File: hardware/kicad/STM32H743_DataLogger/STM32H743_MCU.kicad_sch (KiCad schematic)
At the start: 29 parts, among them J10 SWD Debug, J11 USB-C, U10 STM32H743VIT6, Y1 25MHz, Y2 32.768kHz

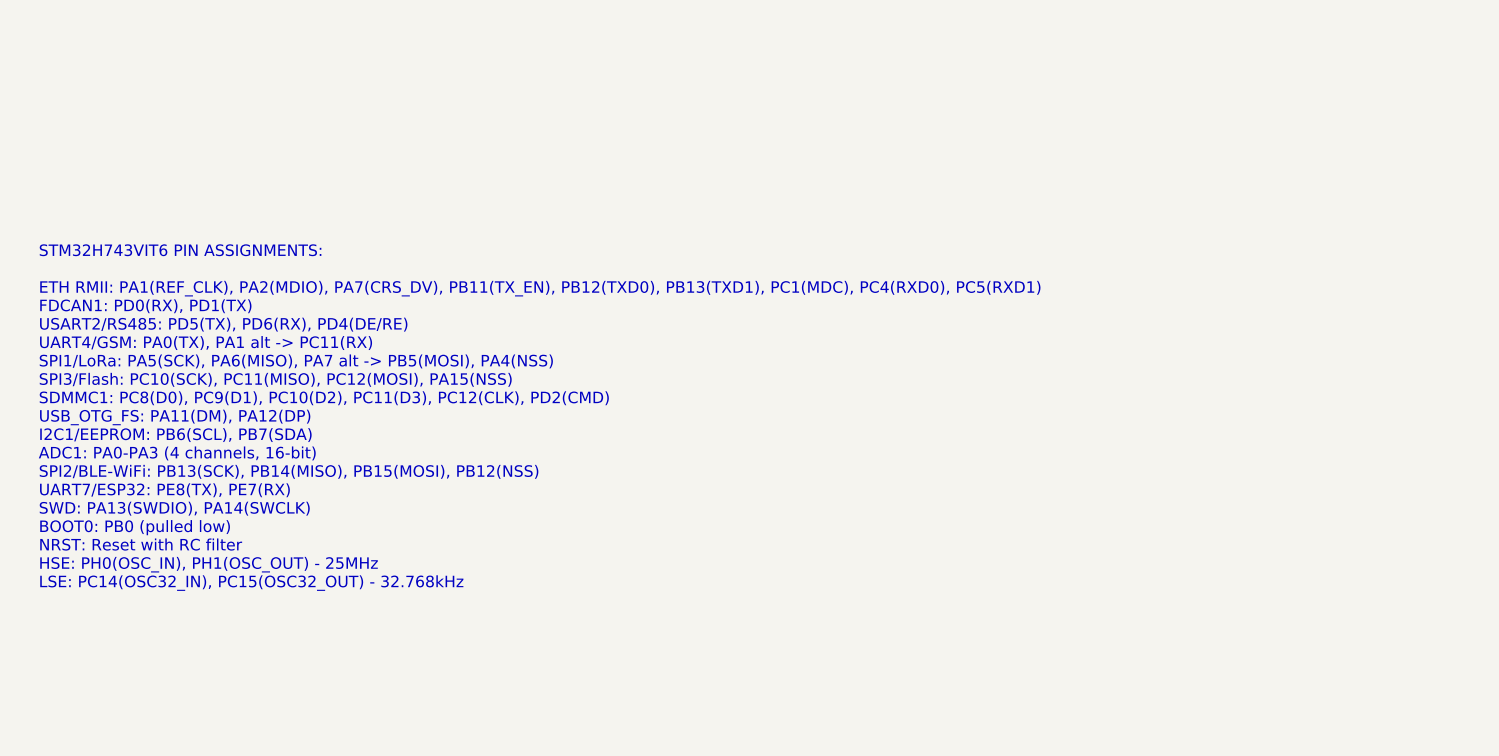
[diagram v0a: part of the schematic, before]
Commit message: feat: Upgrade to full industrial-grade components and SPI architecture
Major design changes for PLC-grade reliability:

Component Upgrades:
- Replace ESP32-C3 dual-MCU with ATWINC1500 WiFi (SPI2) + RN4870 BLE (UART7)
  Eliminates second processor, both rated -40 to +85°C industrial
- Replace LAN8742A RMII PHY with W5500 SPI Ethernet controller
  Hardwired TCP/IP stack, frees 11 RMII pins, simpler firmware
- Replace RFM95W module with SX1276IMLTRT bare IC (-40 to +85°C)
  Full industrial temp range with 32MHz TCXO and custom RF matching
- Add TPS3823-33 external hardware watchdog (1.6s timeout)

Industrial Compliance:
- All key ICs rated -40 to +85°C (industrial grade)
- HumiSeal 1B73 conformal coating spec (MIL-I-46058C)
- EMC compliance targets: IEC 61000-4-2/4/5/6/8
- Ferrite beads on Ethernet pairs for EMI

Architecture: Single MCU (STM32H743) with all peripherals as SPI/UART slaves
- SPI1: SX1276 LoRa
- SPI2: ATWINC1500 WiFi
- SPI3: W25Q64JV Flash
- SPI4: W5500 Ethernet
- UART4: SIM7600G-H GSM/LTE
- UART7: RN4870 BLE

Updated BOM: ~170 components, ~$142/unit (1pc), ~$90/unit (100pc)

https://claude.ai/code/session_01XsiZ6LJT6X46LKY8yEbRbx
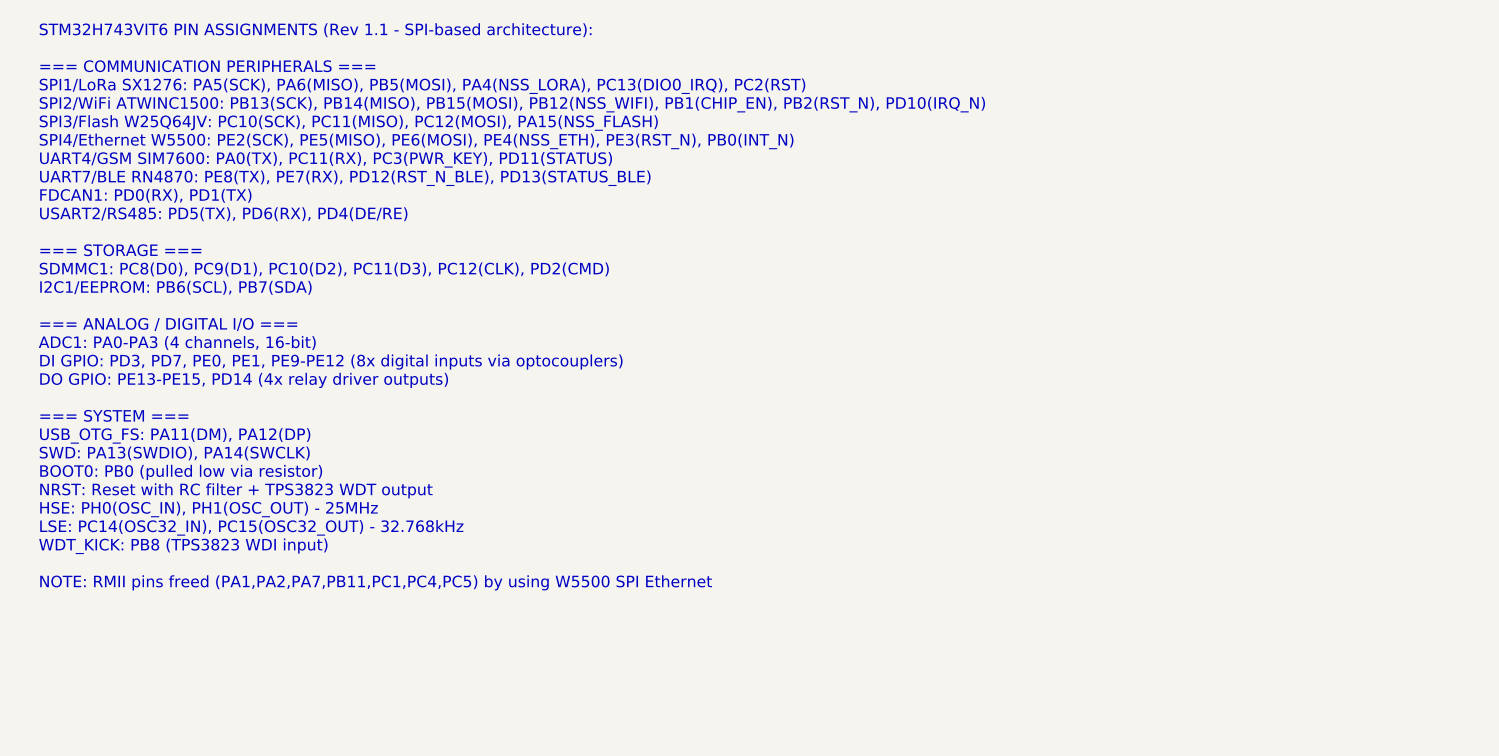
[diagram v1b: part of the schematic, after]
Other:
- note added: "STM32H743VIT6 PIN ASSIGNMENTS (Rev 1.1 - SPI-based architecture): === COMMUNICATION PERIPHERALS === SPI1/LoRa SX1276: PA5(SCK), PA6(MISO), PB5(MOSI), PA4(NSS_LORA), PC13(DIO0_IRQ), PC2(RST) SPI2/WiFi ATWINC1500: PB13(SCK), PB14(MISO), PB15(MOSI), PB12(NSS_WIFI), PB1(CHIP_EN), PB2(RST_N), PD10(IRQ_N) SPI3/Flash W25Q64JV: PC10(SCK), PC11(MISO), PC12(MOSI), PA15(NSS_FLASH) SPI4/Ethernet W5500: PE2(S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"
- note removed: "STM32H743VIT6 PIN ASSIGNMENTS: ETH RMII: PA1(REF_CLK), PA2(MDIO), PA7(CRS_DV), PB11(TX_EN), PB12(TXD0), PB13(TXD1), PC1(MDC), PC4(RXD0), PC5(RXD1) FDCAN1: PD0(RX), PD1(TX) USART2/RS485: PD5(TX), PD6(RX), PD4(DE/RE) UART4/GSM: PA0(TX), PA1 alt -> PC11(RX) SPI1/LoRa: PA5(SCK), PA6(MISO), PA7 alt -> PB5(MOSI), PA4(NSS) SPI3/Flash: PC10(SCK), PC11(MISO), PC12(MOSI), PA15(NSS) SDMMC1: PC8(D0), PC9(D1)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"
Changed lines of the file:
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@@
     (title "STM32H743VIT6 MCU - Core System")
     (date "2026-03-15")
-    (rev "1.0")
+    (rev "1.1")
     (company "SCADA Systems")
     (comment 1 "ARM Cortex-M7 480MHz, 2MB Flash, 1MB RAM")
-    (comment 2 "LQFP-100 package")
+    (comment 2 "LQFP-100 package, SPI-based peripherals (W5500/ATWINC1500/SX1276/RN4870)")
   )
   ;; ============================================================
@@
   ;; PIN ASSIGNMENTS (documented as text annotation)
   ;; ============================================================
-  (text "STM32H743VIT6 PIN ASSIGNMENTS:\n\nETH RMII: PA1(REF_CLK), PA2(MDIO), PA7(CRS_DV), PB11(TX_EN), PB12(TXD0), PB13(TXD1), PC1(MDC), PC4(RXD0), PC5(RXD1)\nFDCAN1: PD0(RX), PD1(TX)\nUSART2/RS485: PD5(TX), PD6(RX), PD4(DE/RE)\nUART4/GSM: PA0(TX), PA1 alt -> PC11(RX)\nSPI1/LoRa: PA5(SCK), PA6(MISO), PA7 alt -> PB5(MOSI), PA4(NSS)\nSPI3/Flash: PC10(SCK), PC11(MISO), PC12(MOSI), PA15(NSS)\nSDMMC1: PC8(D0), PC9(D1), PC10(D2), PC11(D3), PC12(CLK), PD2(CMD)\nUSB_OTG_FS: PA11(DM), PA12(DP)\nI2C1/EEPROM: PB6(SCL), PB7(SDA)\nADC1: PA0-PA3 (4 channels, 16-bit)\nSPI2/BLE-WiFi: PB13(SCK), PB14(MISO), PB15(MOSI), PB12(NSS)\nUART7/ESP32: PE8(TX), PE7(RX)\nSWD: PA13(SWDIO), PA14(SWCLK)\nBOOT0: PB0 (pulled low)\nNRST: Reset with RC filter\nHSE: PH0(OSC_IN), PH1(OSC_OUT) - 25MHz\nLSE: PC14(OSC32_IN), PC15(OSC32_OUT) - 32.768kHz"
+  (text "STM32H743VIT6 PIN ASSIGNMENTS (Rev 1.1 - SPI-based architecture):\n\n=== COMMUNICATION PERIPHERALS ===\nSPI1/LoRa SX1276: PA5(SCK), PA6(MISO), PB5(MOSI), PA4(NSS_LORA), PC13(DIO0_IRQ), PC2(RST)\nSPI2/WiFi ATWINC1500: PB13(SCK), PB14(MISO), PB15(MOSI), PB12(NSS_WIFI), PB1(CHIP_EN), PB2(RST_N), PD10(IRQ_N)\nSPI3/Flash W25Q64JV: PC10(SCK), PC11(MISO), PC12(MOSI), PA15(NSS_FLASH)\nSPI4/Ethernet W5500: PE2(SCK), PE5(MISO), PE6(MOSI), PE4(NSS_ETH), PE3(RST_N), PB0(INT_N)\nUART4/GSM SIM7600: PA0(TX), PC11(RX), PC3(PWR_KEY), PD11(STATUS)\nUART7/BLE RN4870: PE8(TX), PE7(RX), PD12(RST_N_BLE), PD13(STATUS_BLE)\nFDCAN1: PD0(RX), PD1(TX)\nUSART2/RS485: PD5(TX), PD6(RX), PD4(DE/RE)\n\n=== STORAGE ===\nSDMMC1: PC8(D0), PC9(D1), PC10(D2), PC11(D3), PC12(CLK), PD2(CMD)\nI2C1/EEPROM: PB6(SCL), PB7(SDA)\n\n=== ANALOG / DIGITAL I/O ===\nADC1: PA0-PA3 (4 channels, 16-bit)\nDI GPIO: PD3, PD7, PE0, PE1, PE9-PE12 (8x digital inputs via optocouplers)\nDO GPIO: PE13-PE15, PD14 (4x relay driver outputs)\n\n=== SYSTEM ===\nUSB_OTG_FS: PA11(DM), PA12(DP)\nSWD: PA13(SWDIO), PA14(SWCLK)\nBOOT0: PB0 (pulled low via resistor)\nNRST: Reset with RC filter + TPS3823 WDT output\nHSE: PH0(OSC_IN), PH1(OSC_OUT) - 25MHz\nLSE: PC14(OSC32_IN), PC15(OSC32_OUT) - 32.768kHz\nWDT_KICK: PB8 (TPS3823 WDI input)\n\nNOTE: RMII pins freed (PA1,PA2,PA7,PB11,PC1,PC4,PC5) by using W5500 SPI Ethernet"
     (exclude_from_sim no)
     (at 25.4 25.4 0)

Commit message: feat: Add programming interface headers (J12-J14) to PCB
Schematic additions (STM32H743_MCU.kicad_sch):
- J12: UART debug console header (4-pin 2.54mm: VCC/TX/RX/GND)
  USART1 on PA9(TX)/PA10(RX) at 115200 baud, FTDI cable compatible
  33R series resistors (R14/R15) for ESD protection
- J13: BOOT0 select jumper (3-pin: GND-BOOT0-3V3)
  GND position = normal flash boot (default via R16 10k pull-down)
  3V3 position = DFU bootloader mode for USB/UART programming
- J14: Tag-Connect TC2050-IDC pads (10-pin pogo-pin footprint)
  Same SWD signals as J10, zero per-board connector cost
  For production/factory programming

Firmware additions:
- debug_console.rs: UART console driver with boot banner, periodic
  status reports, log levels, and simple command parser for field
  diagnostics (status/sdinfo/alarms/links/version/reset/help)
- debug_console_task: Embassy async task outputting diagnostics on J12
- uart_ports.rs: Added USART1 debug console config (115200 baud)
- Updated pin assignment docs to Rev 1.2

https://claude.ai/code/session_01XsiZ6LJT6X46LKY8yEbRbx
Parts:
- added J12: UART Debug Console, Connector_PinHeader_2.54mm:PinHeader_1x04_P2.54mm_Vertical, symbol Connector_Generic:Conn_01x04
- added J13: BOOT0 Select, Connector_PinHeader_2.54mm:PinHeader_1x03_P2.54mm_Vertical, symbol Connector_Generic:Conn_01x03
- added J14: TC2050-IDC SWD, Connector:Tag-Connect_TC2050-IDC-FP_2x05_P1.27mm_Vertical, symbol Connector:Tag-Connect_TC2050-IDC
- added R14, R15: 33R, Resistor_SMD:R_0402_1005Metric, symbol Device:R
- added R16: 10k, Resistor_SMD:R_0402_1005Metric, symbol Device:R
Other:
- note added: "STM32H743VIT6 PIN ASSIGNMENTS (Rev 1.2 - SPI-based architecture): === COMMUNICATION PERIPHERALS === SPI1/LoRa SX1276: PA5(SCK), PA6(MISO), PB5(MOSI), PA4(NSS_LORA), PC13(DIO0_IRQ), PC2(RST) SPI2/WiFi ATWINC1500: PB13(SCK), PB14(MISO), PB15(MOSI), PB12(NSS_WIFI), PB1(CHIP_EN), PC0(RST_N), PD10(IRQ_N) SPI3/Flash W25Q64JV: PB3(SCK), PB4(MISO), PB2(MOSI), PA15(NSS_FLASH) [REMAPPED from PC10-12 for SD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"
- note removed: "STM32H743VIT6 PIN ASSIGNMENTS (Rev 1.1 - SPI-based architecture): === COMMUNICATION PERIPHERALS === SPI1/LoRa SX1276: PA5(SCK), PA6(MISO), PB5(MOSI), PA4(NSS_LORA), PC13(DIO0_IRQ), PC2(RST) SPI2/WiFi ATWINC1500: PB13(SCK), PB14(MISO), PB15(MOSI), PB12(NSS_WIFI), PB1(CHIP_EN), PB2(RST_N), PD10(IRQ_N) SPI3/Flash W25Q64JV: PC10(SCK), PC11(MISO), PC12(MOSI), PA15(NSS_FLASH) SPI4/Ethernet W5500: PE2(S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"
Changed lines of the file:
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@@
+  )
+  ;; ============================================================
+  ;; UART DEBUG CONSOLE HEADER (J12)
+  ;; 4-pin 2.54mm header: VCC(3.3V), TX(PA9), RX(PA10), GND
+  ;; USART1 at 115200 baud for debug/diagnostic output
+  ;; Compatible with standard FTDI USB-UART cables
+  ;; ============================================================
+  (symbol
+    (lib_id "Connector_Generic:Conn_01x04")
+    (at 254.0 101.6)
+    (unit 1)
+    (exclude_from_sim no)
+    (in_bom yes)
+    (on_board yes)
+    (dnp no)
+    (uuid "MCU-0090-J12")
+    (property "Reference" "J12"
+      (at 254.0 92.71 0)
+      (effects (font (size 1.27 1.27)))
+    )
+    (property "Value" "UART Debug Console"
+      (at 254.0 95.25 0)
+      (effects (font (size 1.27 1.27)))
+    )
+    (property "Footprint" "Connector_PinHeader_2.54mm:PinHeader_1x04_P2.54mm_Vertical"
+      (at 254.0 101.6 0)
+      (effects (font (size 1.27 1.27)) hide)
+    )
+    (property "MPN" "PinHeader_1x04_P2.54mm"
+      (at 254.0 101.6 0)
+      (effects (font (size 1.27 1.27)) hide)
+    )
+    (property "Manufacturer" "Generic"
+      (at 254.0 101.6 0)
+      (effects (font (size 1.27 1.27)) hide)
+    )
+    (pin "1" (uuid "J12-pin1-uuid") (name "VCC_3V3"))
+    (pin "2" (uuid "J12-pin2-uuid") (name "USART1_TX (PA9)"))
+    (pin "3" (uuid "J12-pin3-uuid") (name "USART1_RX (PA10)"))
+    (pin "4" (uuid "J12-pin4-uuid") (name "GND"))
+  )
+  ;; ESD protection on UART debug header
+  (symbol (lib_id "Device:R") (at 248.92 101.6) (unit 1)
+    (exclude_from_sim no) (in_bom yes) (on_board yes) (dnp no)
+    (uuid "MCU-0091-R14")
+    (property "Reference" "R14" (at 246.38 100.33 0) (effects (font (size 1.27 1.27))))
+    (property "Value" "33R" (at 248.92 104.14 0) (effects (font (size 1.27 1.27))))
+    (property "Footprint" "Resistor_SMD:R_0402_1005Metric" (at 248.92 101.6 0) (effects (font (size 1.27 1.27)) hide))
+    (property "MPN" "RC0402FR-0733RL" (at 248.92 101.6 0) (effects (font (size 1.27 1.27)) hide))
+    (property "Manufacturer" "Yageo" (at 248.92 101.6 0) (effects (font (size 1.27 1.27)) hide))
+  )
+  (symbol (lib_id "Device:R") (at 248.92 107.95) (unit 1)
+    (exclude_from_sim no) (in_bom yes) (on_board yes) (dnp no)
+    (uuid "MCU-0092-R15")
+    (property "Reference" "R15" (at 246.38 106.68 0) (effects (font (size 1.27 1.27))))
+    (property "Value" "33R" (at 248.92 110.49 0) (effects (font (size 1.27 1.27))))
+    (property "Footprint" "Resistor_SMD:R_0402_1005Metric" (at 248.92 107.95 0) (effects (font (size 1.27 1.27)) hide))
+    (property "MPN" "RC0402FR-0733RL" (at 248.92 107.95 0) (effects (font (size 1.27 1.27)) hide))
+    (property "Manufacturer" "Yageo" (at 248.92 107.95 0) (effects (font (size 1.27 1.27)) hide))
+  )
+  ;; ============================================================
+  ;; BOOT0 SELECT HEADER (J13)
+  ;; 1x3 2.54mm jumper: GND-BOOT0-3V3
+  ;; Center pin to BOOT0, jumper to GND=normal flash boot,
+  ;; jumper to 3V3=DFU bootloader mode (USB/UART programming)
+  ;; ============================================================
+  (symbol
+    (lib_id "Connector_Generic:Conn_01x03")
+    (at 254.0 120.65)
+    (unit 1)
+    (exclude_from_sim no)
+    (in_bom yes)
+    (on_board yes)
+    (dnp no)
+    (uuid "MCU-0095-J13")
+    (property "Reference" "J13"
+      (at 254.0 113.03 0)
+      (effects (font (size 1.27 1.27)))
+    )
+    (property "Value" "BOOT0 Select"
+      (at 254.0 115.57 0)
+      (effects (font (size 1.27 1.27)))
+    )
+    (property "Footprint" "Connector_PinHeader_2.54mm:PinHeader_1x03_P2.54mm_Vertical"
+      (at 254.0 120.65 0)
+      (effects (font (size 1.27 1.27)) hide)
+    )
+    (property "MPN" "PinHeader_1x03_P2.54mm"
+      (at 254.0 120.65 0)
+      (effects (font (size 1.27 1.27)) hide)
+    )
+    (property "Manufacturer" "Generic"
+      (at 254.0 120.65 0)
+      (effects (font (size 1.27 1.27)) hide)
+    )
+    (pin "1" (uuid "J13-pin1-uuid") (name "GND (Normal Boot)"))
+    (pin "2" (uuid "J13-pin2-uuid") (name "BOOT0"))
+    (pin "3" (uuid "J13-pin3-uuid") (name "VCC_3V3 (DFU Mode)"))
+  )
+  ;; BOOT0 pull-down (default normal boot even without jumper)
+  (symbol (lib_id "Device:R") (at 248.92 120.65) (unit 1)
+    (exclude_from_sim no) (in_bom yes) (on_board yes) (dnp no)
+    (uuid "MCU-0096-R16")
+    (property "Reference" "R16" (at 246.38 119.38 0) (effects (font (size 1.27 1.27))))
+    (property "Value" "10k" (at 248.92 123.19 0) (effects (font (size 1.27 1.27))))
+    (property "Footprint" "Resistor_SMD:R_0402_1005Metric" (at 248.92 120.65 0) (effects (font (size 1.27 1.27)) hide))
+    (property "MPN" "RC0402FR-0710KL" (at 248.92 120.65 0) (effects (font (size 1.27 1.27)) hide))
+    (property "Manufacturer" "Yageo" (at 248.92 120.65 0) (effects (font (size 1.27 1.27)) hide))
+  )
+  ;; ============================================================
+  ;; TAG-CONNECT TC2050-IDC PROGRAMMING PADS (J14)
+  ;; 10-pin pogo-pin footprint for production/factory programming
+  ;; Same SWD signals as J10 but with space-efficient pads
+  ;; No connector cost per board - just PCB pads
+  ;; ============================================================
+  (symbol
+    (lib_id "Connector:Tag-Connect_TC2050-IDC")
+    (at 254.0 143.51)
+    (unit 1)
+    (exclude_from_sim no)
+    (in_bom yes)
+    (on_board yes)
+    (dnp no)
+    (uuid "MCU-0100-J14")
+    (property "Reference" "J14"
+      (at 254.0 130.81 0)
+      (effects (font (size 1.27 1.27)))
+    )
+    (property "Value" "TC2050-IDC SWD"
+      (at 254.0 133.35 0)
+      (effects (font (size 1.27 1.27)))
+    )
+    (property "Footprint" "Connector:Tag-Connect_TC2050-IDC-FP_2x05_P1.27mm_Vertical"
+      (at 254.0 143.51 0)
+      (effects (font (size 1.27 1.27)) hide)
+    )
+    (property "MPN" "TC2050-IDC"
+      (at 254.0 143.51 0)
+      (effects (font (size 1.27 1.27)) hide)
+    )
+    (property "Manufacturer" "Tag-Connect"
+      (at 254.0 143.51 0)
+      (effects (font (size 1.27 1.27)) hide)
+    )
   )
   ;; ============================================================
@@
   ;; PIN ASSIGNMENTS (documented as text annotation)
   ;; ============================================================
-  (text "STM32H743VIT6 PIN ASSIGNMENTS (Rev 1.1 - SPI-based architecture):\n\n=== COMMUNICATION PERIPHERALS ===\nSPI1/LoRa SX1276: PA5(SCK), PA6(MISO), PB5(MOSI), PA4(NSS_LORA), PC13(DIO0_IRQ), PC2(RST)\nSPI2/WiFi ATWINC1500: PB13(SCK), PB14(MISO), PB15(MOSI), PB12(NSS_WIFI), PB1(CHIP_EN), PB2(RST_N), PD10(IRQ_N)\nSPI3/Flash W25Q64JV: PC10(SCK), PC11(MISO), PC12(MOSI), PA15(NSS_FLASH)\nSPI4/Ethernet W5500: PE2(SCK), PE5(MISO), PE6(MOSI), PE4(NSS_ETH), PE3(RST_N), PB0(INT_N)\nUART4/GSM SIM7600: PA0(TX), PC11(RX), PC3(PWR_KEY), PD11(STATUS)\nUART7/BLE RN4870: PE8(TX), PE7(RX), PD12(RST_N_BLE), PD13(STATUS_BLE)\nFDCAN1: PD0(RX), PD1(TX)\nUSART2/RS485: PD5(TX), PD6(RX), PD4(DE/RE)\n\n=== STORAGE ===\nSDMMC1: PC8(D0), PC9(D1), PC10(D2), PC11(D3), PC12(CLK), PD2(CMD)\nI2C1/EEPROM: PB6(SCL), PB7(SDA)\n\n=== ANALOG / DIGITAL I/O ===\nADC1: PA0-PA3 (4 channels, 16-bit)\nDI GPIO: PD3, PD7, PE0, PE1, PE9-PE12 (8x digital inputs via optocouplers)\nDO GPIO: PE13-PE15, PD14 (4x relay driver outputs)\n\n=== SYSTEM ===\nUSB_OTG_FS: PA11(DM), PA12(DP)\nSWD: PA13(SWDIO), PA14(SWCLK)\nBOOT0: PB0 (pulled low via resistor)\nNRST: Reset with RC filter + TPS3823 WDT output\nHSE: PH0(OSC_IN), PH1(OSC_OUT) - 25MHz\nLSE: PC14(OSC32_IN), PC15(OSC32_OUT) - 32.768kHz\nWDT_KICK: PB8 (TPS3823 WDI input)\n\nNOTE: RMII pins freed (PA1,PA2,PA7,PB11,PC1,PC4,PC5) by using W5500 SPI Ethernet"
+  (text "STM32H743VIT6 PIN ASSIGNMENTS (Rev 1.2 - SPI-based architecture):\n\n=== COMMUNICATION PERIPHERALS ===\nSPI1/LoRa SX1276: PA5(SCK), PA6(MISO), PB5(MOSI), PA4(NSS_LORA), PC13(DIO0_IRQ), PC2(RST)\nSPI2/WiFi ATWINC1500: PB13(SCK), PB14(MISO), PB15(MOSI), PB12(NSS_WIFI), PB1(CHIP_EN), PC0(RST_N), PD10(IRQ_N)\nSPI3/Flash W25Q64JV: PB3(SCK), PB4(MISO), PB2(MOSI), PA15(NSS_FLASH) [REMAPPED from PC10-12 for SDMMC1]\nSPI4/Ethernet W5500: PE2(SCK), PE5(MISO), PE6(MOSI), PE4(NSS_ETH), PE3(RST_N), PB0(INT_N)\nUSART1/Debug Console: PA9(TX), PA10(RX) -> J12 header (115200 baud)\nUART4/GSM SIM7600: PA0(TX), PC11(RX), PC3(PWR_KEY), PD11(STATUS)\nUART7/BLE RN4870: PE8(TX), PE7(RX), PD12(RST_N_BLE), PD13(STATUS_BLE)\nFDCAN1: PD0(RX), PD1(TX)\nUSART2/RS485: PD5(TX), PD6(RX), PD4(DE/RE)\n\n=== STORAGE ===\nSDMMC1 (4-bit): PC8(D0), PC9(D1), PC10(D2), PC11(D3), PC12(CLK), PD2(CMD)\nI2C1/EEPROM: PB6(SCL), PB7(SDA)\n\n=== ANALOG / DIGITAL I/O ===\nADC1: PA0-PA3 (4 channels, 16-bit)\nDI GPIO: PD3, PD7, PE0, PE1, PE9-PE12 (8x digital inputs via optocouplers)\nDO GPIO: PE13-PE15, PD14 (4x relay driver outputs)\n\n=== SYSTEM ===\nUSB_OTG_FS: PA11(DM), PA12(DP)\nSWD: PA13(SWDIO), PA14(SWCLK)\nBOOT0: Dedicated pin, jumper J13 (GND=flash boot, 3V3=DFU mode), R16 10k pull-down default\nNRST: Reset with RC filter + TPS3823 WDT output\nHSE: PH0(OSC_IN), PH1(OSC_OUT) - 25MHz\nLSE: PC14(OSC32_IN), PC15(OSC32_OUT) - 32.768kHz\nWDT_KICK: PB8 (TPS3823 WDI input)\n\n=== PROGRAMMING INTERFACES ===\nJ10: 10-pin ARM SWD header (Samtec FTSH-105-01-L-DV-K, 1.27mm pitch)\nJ11: USB-C connector (USB_OTG_FS for DFU programming)\nJ12: UART debug console header (4-pin 2.54mm: VCC/TX/RX/GND, USART1 PA9/PA10)\nJ13: BOOT0 select jumper (3-pin: GND-BOOT0-3V3, default=flash boot)\nJ14: Tag-Connect TC2050-IDC pads (production programming, same SWD signals as J10)\n\nNOTE: RMII pins freed (PA1,PA2,PA7,PB11,PC1,PC4,PC5) by using W5500 SPI Ethernet\nNOTE: SPI3 remapped from PC10-12 to PB3/PB4/PB2 to free PC8-12 for SDMMC1 4-bit SD card"
     (exclude_from_sim no)
     (at 25.4 25.4 0)

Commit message: feat: Add P9E silkscreen branding, fix BOM/schematic cross-check issues
- Add complete silkscreen: P9E branding (3.5mm bold), company name,
  website, product info (Weather Station v2.0), functional area labels,
  connector pin labels, LED labels, compliance marks on back
- Fix BOM: add missing J12/J13/J14/R14-R16, resolve LED4 duplicate
  (renamed to LED5 for BLE), fix C101 conflict with C104
- Complete analog input schematic channels 1-3 (TVS, precision resistors,
  anti-alias RC filter, OPA2376 U21 for Ch2-3)
- Complete digital I/O schematic: add optocouplers U32-U37, current
  limiting resistors, pull-ups R38-R44 for DI Ch1-7, relays K2-K4
- Rebrand all files from SCADA Systems to P9E Microsystems Pvt Ltd
- Update revision to 2.0, date to 2026-03-20

https://claude.ai/code/session_01XsiZ6LJT6X46LKY8yEbRbx
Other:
- company: SCADA Systems -> P9E Microsystems Pvt Ltd
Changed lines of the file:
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@@
     (date "2026-03-15")
     (rev "1.1")
-    (company "SCADA Systems")
+    (company "P9E Microsystems Pvt Ltd")
     (comment 1 "ARM Cortex-M7 480MHz, 2MB Flash, 1MB RAM")
     (comment 2 "LQFP-100 package, SPI-based peripherals (W5500/ATWINC1500/SX1276/RN4870)")
